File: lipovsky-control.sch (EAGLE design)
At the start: 46 parts, among them J1 JUMPER-PAD, J5 AVRISP0.1", P1 M04-929P, P2 M04-929P, P3 M04-929P, P4 M04-929P, U1 ATTINYX4A8MU, U2 MIC2288YD5, U3 MIC2288YD5, U4 LTV-816S

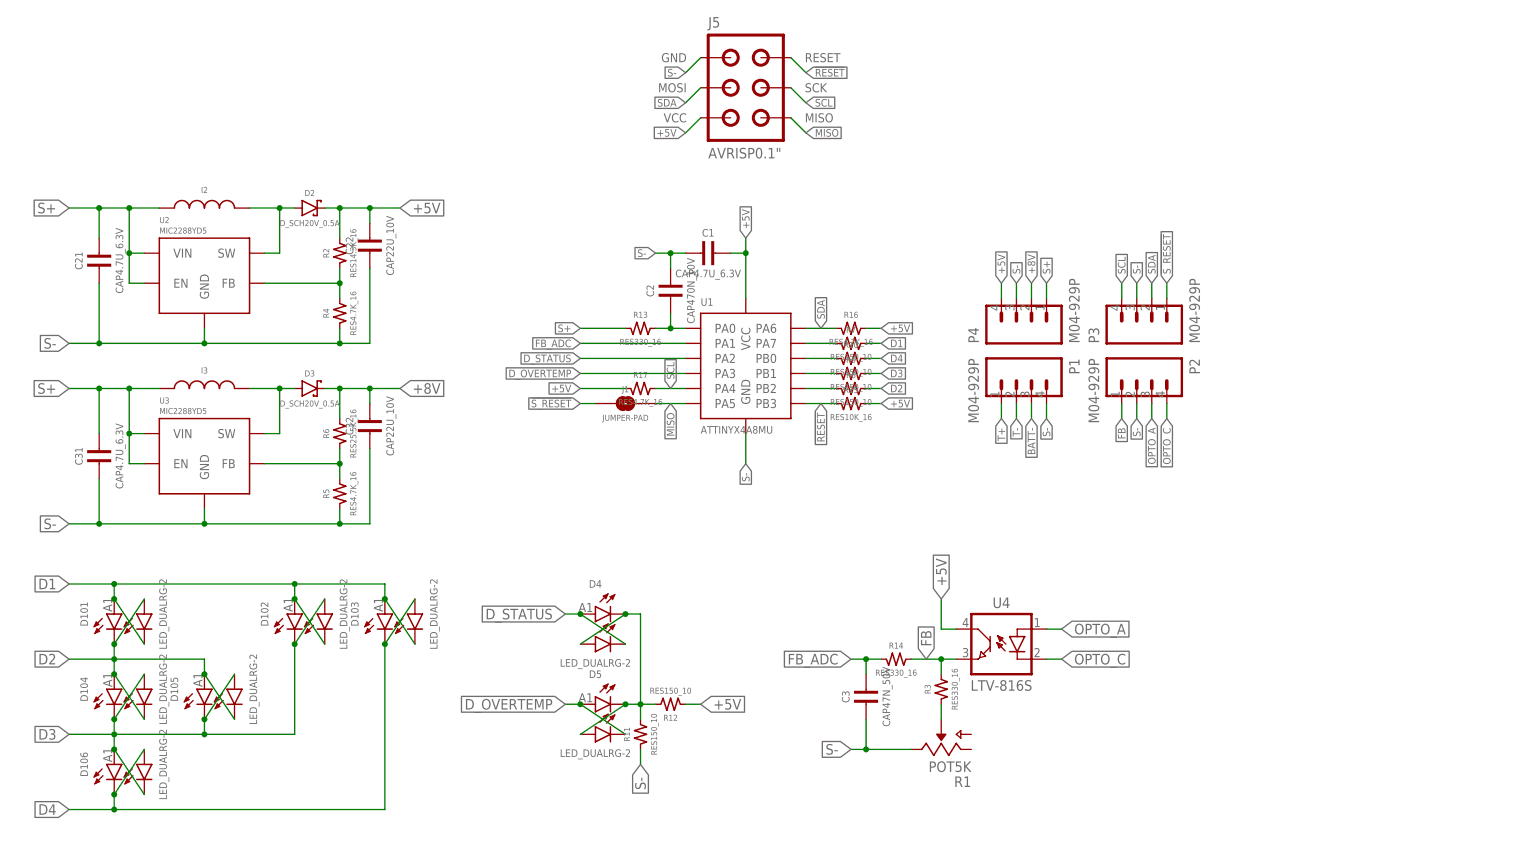
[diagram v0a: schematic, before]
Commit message: Control board compacted
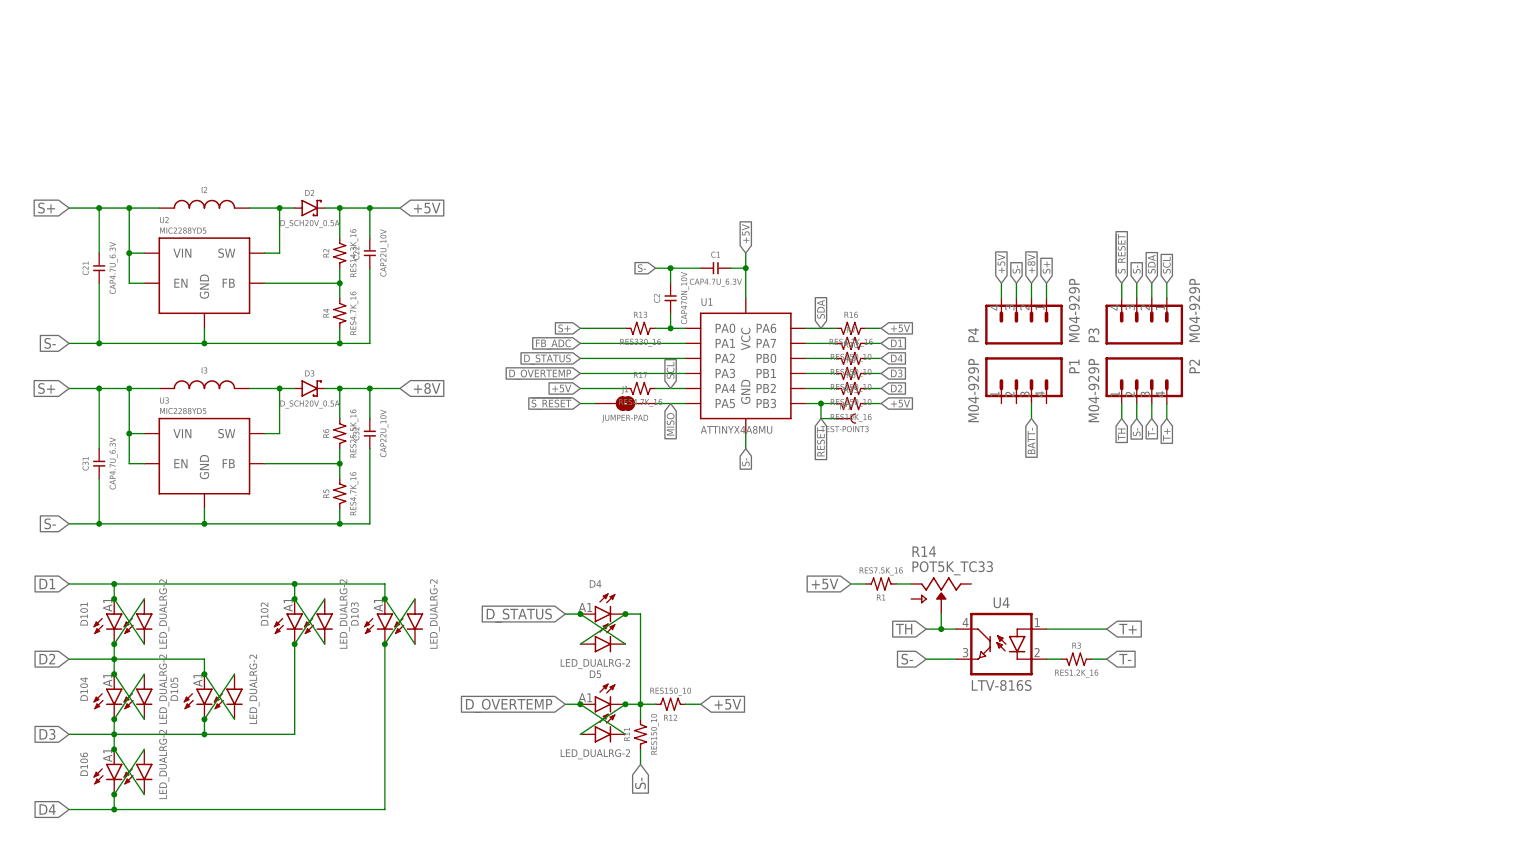
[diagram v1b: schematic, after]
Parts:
- removed C3: CAP47N_50V, dubec:CAP47N_50V
- removed J5: AVRISP0.1", dubec:AVRISP0.1"
- added TP1: TEST-POINT3, SparkFun-Passives:TEST-POINT3
- R1: value POT5K -> RES7.5K_16; device dubec:POT5K -> dubec:RES7.5K_16
- R14: value RES330_16 -> POT5K_TC33; device dubec:RES330_16 -> dubec:POT5K_TC33
- R3: value RES330_16 -> RES1.2K_16; device dubec:RES330_16 -> dubec:RES1.2K_16
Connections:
- removed net FB: P2.1, R14.2, R3.2, U4.E
- removed net OPTO_A: P2.3, U4.A
- removed net OPTO_C: P2.4, U4.K
- new net N$8: R1.1, R14.CCW
- new net TH: P2.1, R14.WIPER, U4.C
- net !RESET: now also TP1.1; no longer J5.RESET
- net !S_RESET: now also P3.4; no longer P3.1
- net +5V: now also R1.2; no longer J5.VCC, U4.C
- net FB_ADC: no longer C3.2, R14.1
- net MISO: no longer J5.MISO
- net N$1: now also U4.K; no longer R1.WIPER
- net S-: now also U4.E; no longer C3.1, J5.GND, P1.4, R1.CW
- net SCL: now also P3.1; no longer J5.SCK, P3.4
- net SDA: no longer J5.MOSI
- net T+: now also P2.4, U4.A; no longer P1.1
- net T-: now also P2.3, R3.2; no longer P1.2
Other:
- moved on the sheet: R3

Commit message: Control board fixes
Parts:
- R1: value RES7.5K_16 -> RES348_16; device dubec:RES7.5K_16 -> dubec:RES348_16
- R14: value POT5K_TC33 -> POT200; device dubec:POT5K_TC33 -> dubec:POT200
- R3: value RES1.2K_16 -> RES470_16; device dubec:RES1.2K_16 -> dubec:RES470_16
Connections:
- removed net FB_ADC: U1.PA1
- net D3: no longer D105.A2, D105.C1
- net D4: now also D105.A2, D105.C1
- net TH: now also U1.PA1
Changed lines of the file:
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@@
 <part name="J1" library="dubec" deviceset="JUMPER-PAD" device=""/>
 <part name="TP1" library="SparkFun-Passives" deviceset="TEST-POINT" device="3"/>
-<part name="R1" library="dubec" deviceset="RES" device="7.5K_16"/>
-<part name="R3" library="dubec" deviceset="RES" device="1.2K_16"/>
-<part name="R14" library="dubec" deviceset="POT" device="5K_TC33"/>
+<part name="R1" library="dubec" deviceset="RES" device="348_16" value="RES348_16"/>
+<part name="R3" library="dubec" deviceset="RES" device="470_16" value="RES470_16"/>
+<part name="R14" library="dubec" deviceset="POT" device="200" value="POT200"/>
 </parts>
 <sheets>
@@
 <label x="-91.44" y="-40.64" size="1.778" layer="95" rot="R180" xref="yes"/>
 <wire x1="-91.44" y1="-40.64" x2="-83.82" y2="-40.64" width="0.1524" layer="91"/>
-<wire x1="-83.82" y1="-40.64" x2="-68.58" y2="-40.64" width="0.1524" layer="91"/>
-<wire x1="-68.58" y1="-40.64" x2="-53.34" y2="-40.64" width="0.1524" layer="91"/>
+<wire x1="-83.82" y1="-40.64" x2="-53.34" y2="-40.64" width="0.1524" layer="91"/>
 <pinref part="D104" gate="G$1" pin="C1"/>
 <wire x1="-83.82" y1="-40.64" x2="-83.82" y2="-38.1" width="0.1524" layer="91"/>
@@
 <wire x1="-83.82" y1="-43.18" x2="-78.74" y2="-50.8" width="0.1524" layer="91"/>
 <junction x="-83.82" y="-43.18"/>
-<pinref part="D105" gate="G$1" pin="C1"/>
-<wire x1="-68.58" y1="-40.64" x2="-68.58" y2="-38.1" width="0.1524" layer="91"/>
-<junction x="-68.58" y="-40.64"/>
-<pinref part="D105" gate="G$1" pin="A2"/>
-<wire x1="-68.58" y1="-38.1" x2="-63.5" y2="-30.48" width="0.1524" layer="91"/>
-<junction x="-68.58" y="-38.1"/>
 <pinref part="D102" gate="G$1" pin="C1"/>
 <wire x1="-53.34" y1="-40.64" x2="-53.34" y2="-25.4" width="0.1524" layer="91"/>
@@
 <segment>
 <label x="-91.44" y="-53.34" size="1.778" layer="95" rot="R180" xref="yes"/>
-<wire x1="-38.1" y1="-53.34" x2="-83.82" y2="-53.34" width="0.1524" layer="91"/>
+<wire x1="-38.1" y1="-53.34" x2="-68.58" y2="-53.34" width="0.1524" layer="91"/>
+<wire x1="-68.58" y1="-53.34" x2="-83.82" y2="-53.34" width="0.1524" layer="91"/>
 <wire x1="-83.82" y1="-53.34" x2="-91.44" y2="-53.34" width="0.1524" layer="91"/>
 <pinref part="D106" gate="G$1" pin="C1"/>
@@
 <wire x1="-38.1" y1="-25.4" x2="-33.02" y2="-17.78" width="0.1524" layer="91"/>
 <junction x="-38.1" y="-25.4"/>
+<pinref part="D105" gate="G$1" pin="A2"/>
+<pinref part="D105" gate="G$1" pin="C1"/>
+<wire x1="-68.58" y1="-38.1" x2="-63.5" y2="-30.48" width="0.1524" layer="91"/>
+<wire x1="-68.58" y1="-38.1" x2="-68.58" y2="-53.34" width="0.1524" layer="91"/>
+<junction x="-68.58" y="-38.1"/>
+<junction x="-68.58" y="-53.34"/>
 </segment>
 <segment>
@@
 </segment>
 </net>
-<net name="FB_ADC" class="0">
-<segment>
-<pinref part="U1" gate="G$1" pin="PA1"/>
-<wire x1="12.7" y1="25.4" x2="-5.08" y2="25.4" width="0.1524" layer="91"/>
-<label x="-5.08" y="25.4" size="1.27" layer="95" rot="R180" xref="yes"/>
-</segment>
-</net>
 <net name="S_ADC" class="0">
 <segment>
@@
 <label x="86.36" y="12.7" size="1.27" layer="95" rot="R270" xref="yes"/>
 </segment>
-</net>
+<segment>
+<pinref part="U1" gate="G$1" pin="PA1"/>
+<wire x1="12.7" y1="25.4" x2="-5.08" y2="25.4" width="0.1524" layer="91"/>
+<label x="-5.08" y="25.4" size="1.27" layer="95" rot="R180" xref="yes"/>
+</segment>
+</net>

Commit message: tidy
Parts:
- renumbered I2 to L1, I3 to L2
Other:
- note added: "S-"
- note added: "T+"
- note added: "T-"
- moved on the sheet: C21, C31
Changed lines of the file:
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@@
 <part name="C21" library="dubec" deviceset="CAP" device="4.7U_6.3V"/>
 <part name="C31" library="dubec" deviceset="CAP" device="4.7U_6.3V"/>
-<part name="I2" library="dubec" deviceset="I" device="4.7U_0.12A"/>
-<part name="I3" library="dubec" deviceset="I" device="10U_0.09A"/>
+<part name="L1" library="dubec" deviceset="I" device="4.7U_0.12A"/>
+<part name="L2" library="dubec" deviceset="I" device="10U_0.09A"/>
 <part name="D2" library="dubec" deviceset="D_SCH" device="20V_0.5A"/>
 <part name="D3" library="dubec" deviceset="D_SCH" device="20V_0.5A"/>
@@
 <sheet>
 <plain>
+<text x="68.58" y="12.7" size="1.778" layer="94" align="top-center">T-</text>
+<text x="66.04" y="12.7" size="1.778" layer="94" align="top-center">T+</text>
+<text x="73.66" y="12.7" size="1.778" layer="94" align="top-center">S-</text>
 </plain>
 <instances>
@@
 <instance part="U2" gate="G$1" x="-68.58" y="35.56"/>
 <instance part="U3" gate="G$1" x="-68.58" y="5.08"/>
-<instance part="C21" gate="G$1" x="-86.36" y="38.1" rot="R90"/>
-<instance part="C31" gate="G$1" x="-86.36" y="5.08" rot="R90"/>
-<instance part="I2" gate="G$1" x="-68.58" y="48.26"/>
-<instance part="I3" gate="G$1" x="-68.58" y="17.78"/>
+<instance part="C21" gate="G$1" x="-86.36" y="40.64" rot="R90"/>
+<instance part="C31" gate="G$1" x="-86.36" y="10.16" rot="R90"/>
+<instance part="L1" gate="G$1" x="-68.58" y="48.26"/>
+<instance part="L2" gate="G$1" x="-68.58" y="17.78"/>
 <instance part="D2" gate="G$1" x="-50.8" y="48.26"/>
 <instance part="D3" gate="G$1" x="-50.8" y="17.78"/>
@@
 <pinref part="C21" gate="G$1" pin="1"/>
 <wire x1="-86.36" y1="25.4" x2="-91.44" y2="25.4" width="0.1524" layer="91"/>
-<wire x1="-86.36" y1="25.4" x2="-86.36" y2="35.56" width="0.1524" layer="91"/>
+<wire x1="-86.36" y1="25.4" x2="-86.36" y2="38.1" width="0.1524" layer="91"/>
 <junction x="-86.36" y="25.4"/>
 <pinref part="R4" gate="G$1" pin="1"/>
@@
 <pinref part="C31" gate="G$1" pin="1"/>
 <wire x1="-86.36" y1="-5.08" x2="-91.44" y2="-5.08" width="0.1524" layer="91"/>
-<wire x1="-86.36" y1="2.54" x2="-86.36" y2="-5.08" width="0.1524" layer="91"/>
+<wire x1="-86.36" y1="7.62" x2="-86.36" y2="-5.08" width="0.1524" layer="91"/>
 <junction x="-86.36" y="-5.08"/>
 <label x="-91.44" y="-5.08" size="1.778" layer="95" rot="R180" xref="yes"/>
@@
 </segment>
 <segment>
-<pinref part="I2" gate="G$1" pin="1"/>
+<pinref part="L1" gate="G$1" pin="1"/>
 <wire x1="-76.2" y1="48.26" x2="-81.28" y2="48.26" width="0.1524" layer="91"/>
 <wire x1="-81.28" y1="48.26" x2="-86.36" y2="48.26" width="0.1524" layer="91"/>
@@
 <wire x1="-81.28" y1="35.56" x2="-78.74" y2="35.56" width="0.1524" layer="91"/>
 <pinref part="C21" gate="G$1" pin="2"/>
-<wire x1="-86.36" y1="48.26" x2="-86.36" y2="40.64" width="0.1524" layer="91"/>
+<wire x1="-86.36" y1="48.26" x2="-86.36" y2="43.18" width="0.1524" layer="91"/>
 <junction x="-86.36" y="48.26"/>
 </segment>
 <segment>
-<pinref part="I3" gate="G$1" pin="1"/>
+<pinref part="L2" gate="G$1" pin="1"/>
 <wire x1="-76.2" y1="17.78" x2="-81.28" y2="17.78" width="0.1524" layer="91"/>
 <wire x1="-81.28" y1="17.78" x2="-86.36" y2="17.78" width="0.1524" layer="91"/>
@@
 <junction x="-81.28" y="10.16"/>
 <pinref part="C31" gate="G$1" pin="2"/>
-<wire x1="-86.36" y1="17.78" x2="-86.36" y2="7.62" width="0.1524" layer="91"/>
+<wire x1="-86.36" y1="17.78" x2="-86.36" y2="12.7" width="0.1524" layer="91"/>
 <junction x="-86.36" y="17.78"/>
 <label x="-91.44" y="17.78" size="1.778" layer="95" rot="R180" xref="yes"/>
@@
 <net name="N$4" class="0">
 <segment>
-<pinref part="I2" gate="G$1" pin="2"/>
+<pinref part="L1" gate="G$1" pin="2"/>
 <pinref part="D2" gate="G$1" pin="A"/>
 <wire x1="-60.96" y1="48.26" x2="-55.88" y2="48.26" width="0.1524" layer="91"/>
@@
 <net name="N$9" class="0">
 <segment>
-<pinref part="I3" gate="G$1" pin="2"/>
+<pinref part="L2" gate="G$1" pin="2"/>
 <pinref part="D3" gate="G$1" pin="A"/>
 <wire x1="-60.96" y1="17.78" x2="-55.88" y2="17.78" width="0.1524" layer="91"/>

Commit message: Added choke
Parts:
- added U$2: CHOKE-102-2P, dubec:CHOKE-102-2P
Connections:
- new net S+F: C21.2, C31.2, L1.1, L2.1, U$2.4, U2.EN, U2.VIN, U3.EN, U3.VIN
- new net S-F: C1.1, C21.1, C22.1, C31.1, C32.1, R11.1, R4.1, R5.1, U$2.3, U1.GND, U2.GND, U3.GND
- net S+: now also U$2.1; no longer C21.2, C31.2, L1.1, L2.1, U2.EN, U2.VIN, U3.EN, U3.VIN
- net S-: now also U$2.2; no longer C1.1, C21.1, C22.1, C31.1, C32.1, R11.1, R4.1, R5.1, U1.GND, U2.GND, U3.GND
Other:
- moved on the sheet: C2, P1, P2, P3, P4, R1, R14, R3, U4

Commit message: S-F
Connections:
- net S-: no longer P2.2, P3.3, U4.E
- net S-F: now also P2.2, P3.3, U4.E
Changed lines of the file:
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@@
 <net name="S-" class="0">
-<segment>
-<label x="93.98" y="-7.62" size="1.27" layer="95" rot="R270" xref="yes"/>
-<pinref part="P2" gate="G$1" pin="2"/>
-<wire x1="93.98" y1="-7.62" x2="93.98" y2="-5.08" width="0.1524" layer="91"/>
-</segment>
-<segment>
-<label x="93.98" y="15.24" size="1.27" layer="95" rot="R90" xref="yes"/>
-<pinref part="P3" gate="G$1" pin="3"/>
-<wire x1="93.98" y1="15.24" x2="93.98" y2="12.7" width="0.1524" layer="91"/>
-</segment>
 <segment>
 <label x="73.66" y="15.24" size="1.27" layer="95" rot="R90" xref="yes"/>
 <pinref part="P4" gate="G$1" pin="3"/>
 <wire x1="73.66" y1="15.24" x2="73.66" y2="12.7" width="0.1524" layer="91"/>
-</segment>
-<segment>
-<pinref part="U4" gate="G$1" pin="E"/>
-<wire x1="63.5" y1="-48.26" x2="58.42" y2="-48.26" width="0.1524" layer="91"/>
-<label x="58.42" y="-48.26" size="1.778" layer="95" rot="R180" xref="yes"/>
 </segment>
 <segment>
@@
 <label x="5.08" y="-45.72" size="1.778" layer="95" rot="R270" xref="yes"/>
 </segment>
-</net>
+<segment>
+<pinref part="P3" gate="G$1" pin="3"/>
+<wire x1="93.98" y1="12.7" x2="93.98" y2="15.24" width="0.1524" layer="91"/>
+<label x="93.98" y="15.24" size="1.27" layer="95" rot="R90" xref="yes"/>
+</segment>
+<segment>
+<pinref part="U4" gate="G$1" pin="E"/>
+<wire x1="63.5" y1="-48.26" x2="58.42" y2="-48.26" width="0.1524" layer="91"/>
+<label x="58.42" y="-48.26" size="1.778" layer="95" rot="R180" xref="yes"/>
+</segment>
+<segment>
+<label x="93.98" y="-7.62" size="1.27" layer="95" rot="R270" xref="yes"/>
+<pinref part="P2" gate="G$1" pin="2"/>
+<wire x1="93.98" y1="-7.62" x2="93.98" y2="-5.08" width="0.1524" layer="91"/>
+</segment>
+</net>

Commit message: routing
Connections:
- removed net N$3: R10.1, U1.PB0
- removed net N$5: R8.1, U1.PB2
- removed net N$6: R7.1, U1.PA7
- removed net N$7: R9.1, U1.PB1
- new net D1L: D101.A1, D101.C2, D102.A1, D102.C2, D103.A1, D103.C2, R7.2
- new net D2L: D101.A2, D101.C1, D104.A1, D104.C2, D105.A1, D105.C2, R8.2
- new net D3L: D102.A2, D102.C1, D104.A2, D104.C1, D106.A1, D106.C2, R9.2
- new net D4L: D103.A2, D103.C1, D105.A2, D105.C1, D106.A2, D106.C1, R10.2
- net D1: now also R7.1, U1.PA7; no longer D101.A1, D101.C2, D102.A1, D102.C2, D103.A1, D103.C2, R7.2
- net D2: now also R8.1, U1.PB2; no longer D101.A2, D101.C1, D104.A1, D104.C2, D105.A1, D105.C2, R8.2
- net D3: now also R9.1, U1.PB1; no longer D102.A2, D102.C1, D104.A2, D104.C1, D106.A1, D106.C2, R9.2
- net D4: now also R10.1, U1.PB0; no longer D103.A2, D103.C1, D105.A2, D105.C1, D106.A2, D106.C1, R10.2
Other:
- moved on the sheet: D101, D102, D103, D104, D105, D106, D4, D5, R10, R11, R12, R15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
